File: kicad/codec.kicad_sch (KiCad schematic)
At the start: 8 parts, among them U11 TAC5212

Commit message: layout updates
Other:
- note added: "audio codec"
- note added: "note: inputs are DC coupled"
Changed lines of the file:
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@@
 	(generator_version "10.0")
 	(paper "A4")
+	(text "audio codec"
+		(exclude_from_sim no)
+		(at 216.916 176.53 0)
+		(effects
+			(font
+				(size 2.54 2.54)
+			)
+			(justify left bottom)
+		)
+	)
+	(text "note: inputs are DC coupled"
+		(exclude_from_sim no)
+		(at 51.816 97.79 0)
+		(effects
+			(font
+				(size 1.27 1.27)
+			)
+		)
+	)
 	(junction
 		(at 149.86 102.87)

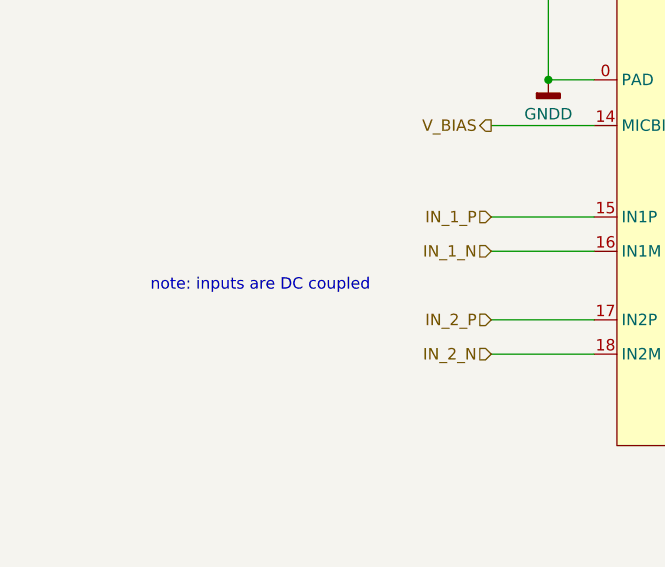
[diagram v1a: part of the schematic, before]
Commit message: ac coupled inputs
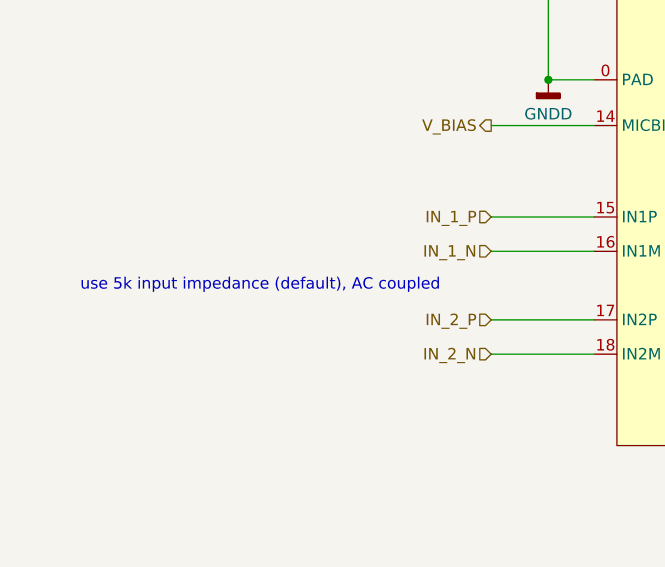
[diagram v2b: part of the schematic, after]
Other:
- note added: "use 5k input impedance (default), AC coupled"
- note removed: "note: inputs are DC coupled"
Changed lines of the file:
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@@
 		)
 	)
-	(text "note: inputs are DC coupled"
+	(text "use 5k input impedance (default), AC coupled"
 		(exclude_from_sim no)
 		(at 51.816 97.79 0)

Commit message: output stage impedances
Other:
- note added: "phone and line outputs are driving 1k impedances. use line out mode for both"
- note added: "use 5k input impedance (default), AC coupled set INCAP_QCHG = 3d (50ms) to match the 40ms charge time of the 10uF cap"
- note removed: "use 5k input impedance (default), AC coupled"
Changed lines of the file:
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@@
 		)
 	)
-	(text "use 5k input impedance (default), AC coupled"
+	(text "phone and line outputs are driving 1k impedances.\nuse line out mode for both"
 		(exclude_from_sim no)
-		(at 51.816 97.79 0)
+		(at 168.656 89.662 0)
 		(effects
 			(font
 				(size 1.27 1.27)
 			)
+			(justify left)
 		)
 	)
+	(text "use 5k input impedance (default), AC coupled\n\nset INCAP_QCHG = 3d (50ms) to match the 40ms charge time of the 10uF cap"
+		(exclude_from_sim no)
+		(at 17.526 117.856 0)
+		(effects
+			(font
+				(size 1.27 1.27)
+			)
+			(justify left)
+		)
+	)

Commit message: #16
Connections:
- net V_BIAS: no longer names the net of U11.14 (MICBIAS)
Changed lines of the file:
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@@
-	(wire
-		(pts
-			(xy 77.47 80.01) (xy 88.9 80.01)
-		)
-		(stroke
-			(width 0)
-			(type default)
-		)
-	)
 	(wire
 		(pts
@@
 		)
 	)
-	(hierarchical_label "V_BIAS"
-		(shape output)
-		(at 77.47 80.01 180)
-		(effects
-			(font
-				(size 1.27 1.27)
-			)
-			(justify right)
-		)
-	)

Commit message: added protection diodes
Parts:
- added D31, D32, D33, D34: BAT54S, Package_TO_SOT_SMD:SOT-23, symbol Diode:BAT54S
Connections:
- net +3V3: now also D31.2 (K), D32.2 (K), D33.2 (K), D34.2 (K)
- net GNDD: no longer C81.1, C82.1, C84.1, U11.0 (PAD)
- net IN_1_N: now also D32.3 (COM)
- net IN_1_P: now also D31.3 (COM)
- net IN_2_P: now also D33.3 (COM)
- new net GNDA: C81.1, C82.1, C84.1, D31.1 (A), D32.1 (A), D33.1 (A), D34.1 (A), U11.0 (PAD)

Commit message: footprint selection
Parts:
- C80, C81, C82, C83, C84, C85, C86: footprint (none) -> Capacitor_SMD:C_0603_1608Metric_Pad1.08x0.95mm_HandSolder

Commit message: footprints
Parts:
- U11: footprint (none) -> openmic:TAC5212
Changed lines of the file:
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@@
 			)
 		)
-		(property "Footprint" ""
+		(property "Footprint" "openmic:TAC5212"
 			(at 116.84 90.17 0)
 			(hide yes)

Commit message: output schematic pdfs
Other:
- note removed: "audio codec"
- company: (none) -> OpenMic
- title: (none) -> Audio codec
- moved on the sheet: C80, C81, C82, C83, C84, C85, C86, D31, D32, D33, D34, U11
